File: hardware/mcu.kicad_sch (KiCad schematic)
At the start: 16 parts, among them U1 RP2350B, U2 W25Q128JVS, Y1 12MHz

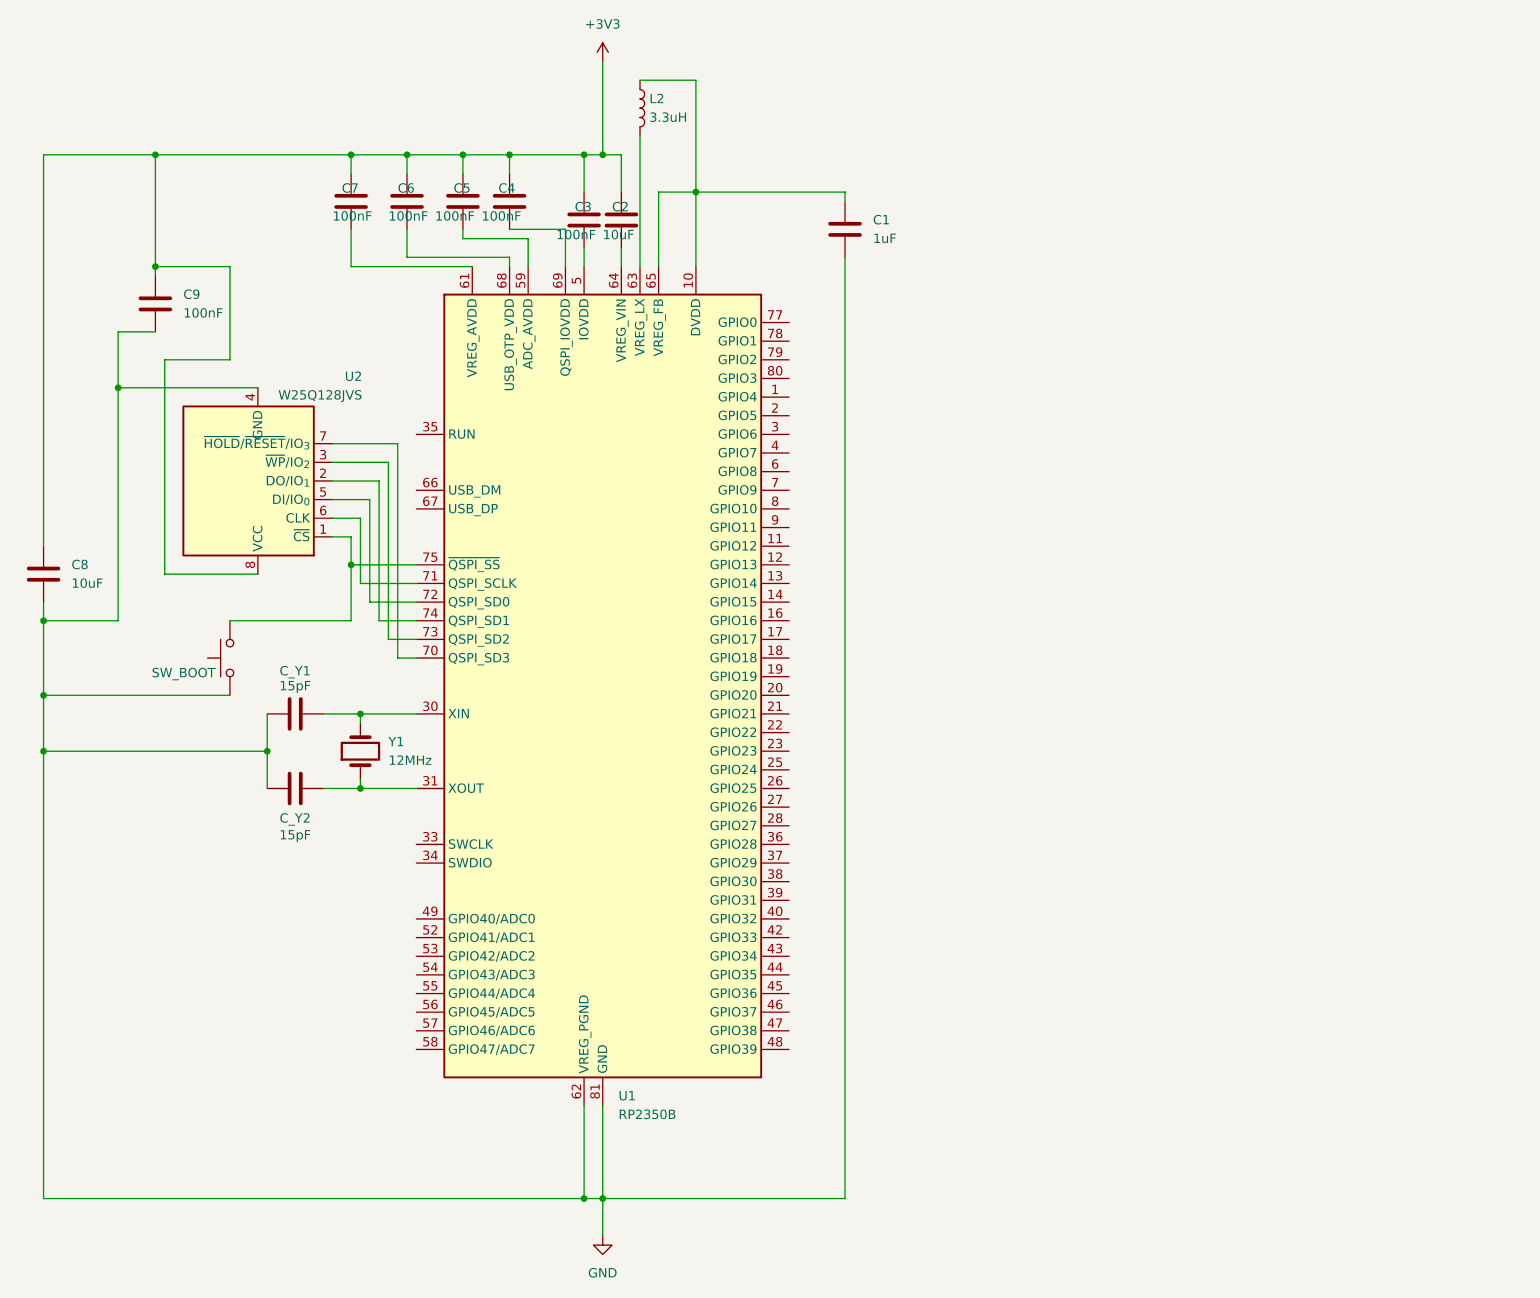
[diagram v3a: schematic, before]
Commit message: add I2C pullups
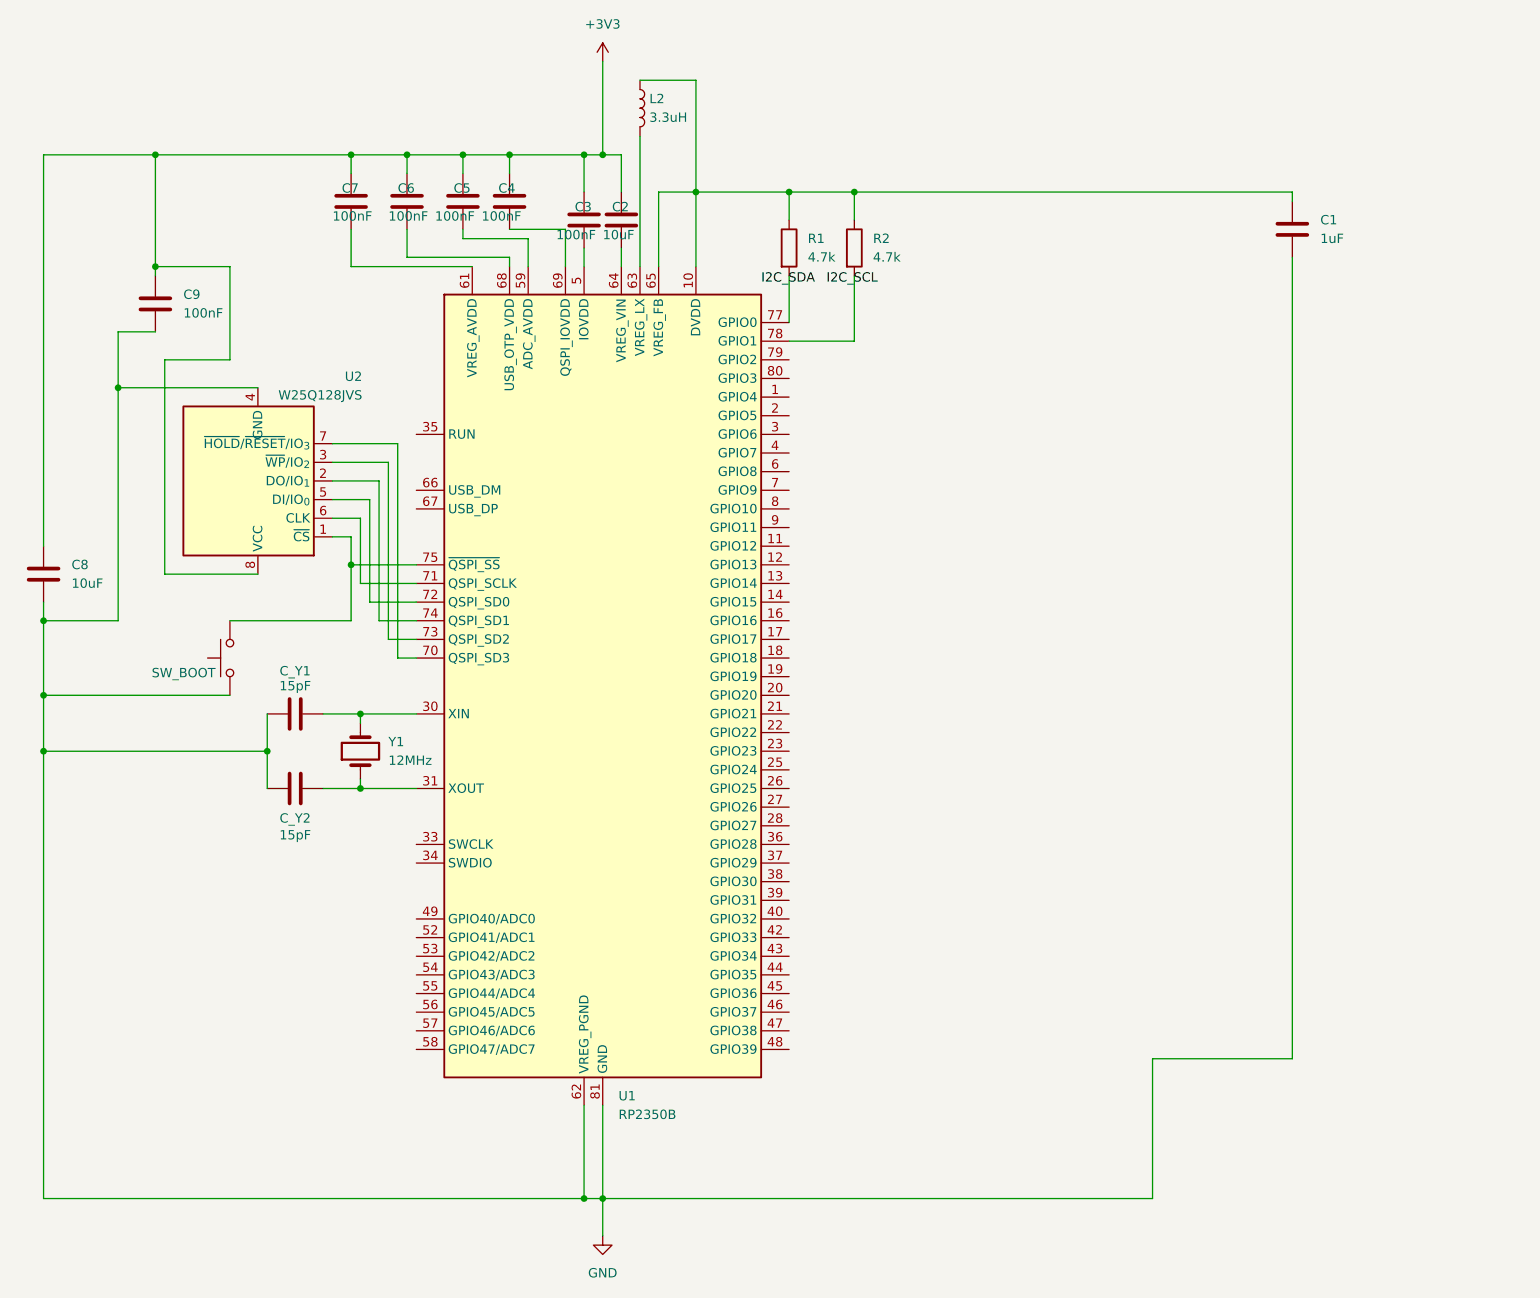
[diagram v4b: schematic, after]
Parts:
- added R1, R2: 4.7k, symbol Device:R
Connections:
- net at C1.1, L2.1, U1.10 (DVDD)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: now also R1.1, R2.1
- net at U1.77 (GPIO0): now also R1.2
- net at U1.78 (GPIO1): now also R2.2
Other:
- moved on the sheet: C1

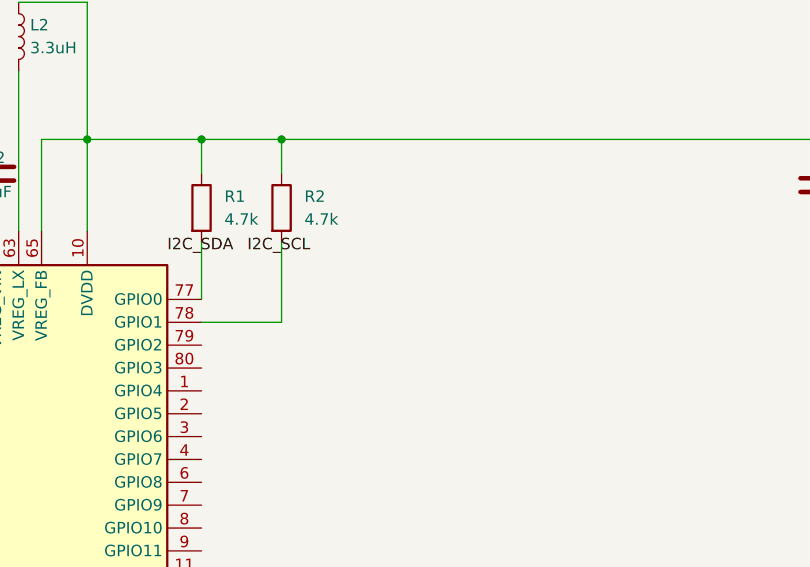
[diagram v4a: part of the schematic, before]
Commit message: add buck/boost
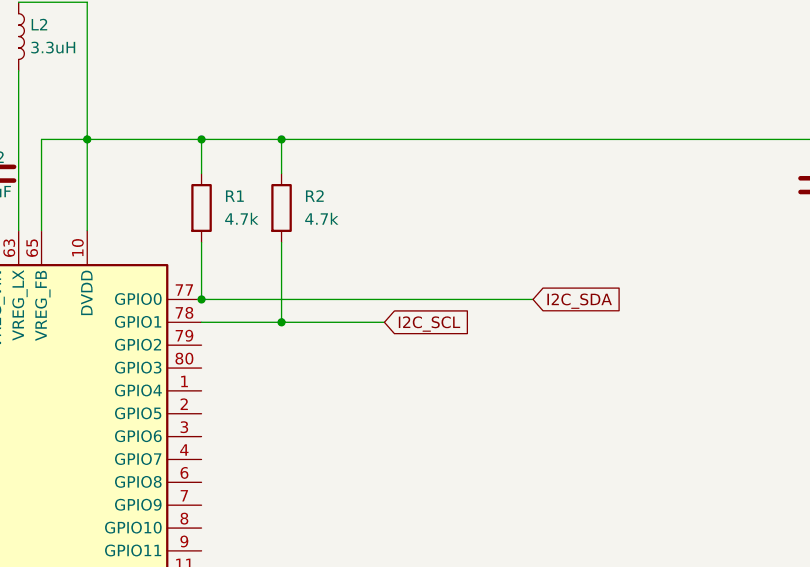
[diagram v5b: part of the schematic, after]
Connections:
- net I2C_SCL: now also R2.2, U1.78 (GPIO1)
- net I2C_SDA: now also R1.2, U1.77 (GPIO0)
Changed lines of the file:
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@@
+	)
+	(junction
+		(at 132.08 60.96)
+		(diameter 0)
+		(color 0 0 0 0)
 	)
 	(junction
@@
 	)
 	(junction
+		(at 123.19 58.42)
+		(diameter 0)
+		(color 0 0 0 0)
+	)
+	(junction
 		(at 85.09 35.56)
 		(diameter 0)
@@
 	(wire
 		(pts
+			(xy 132.08 60.96) (xy 143.51 60.96)
+		)
+		(stroke
+			(width 0)
+			(type default)
+		)
+	)
+	(wire
+		(pts
 			(xy 123.19 40.64) (xy 123.19 44.45)
 		)
@@
 	(wire
 		(pts
+			(xy 123.19 58.42) (xy 160.02 58.42)
+		)
+		(stroke
+			(width 0)
+			(type default)
+		)
+	)
+	(wire
+		(pts
 			(xy 67.31 80.01) (xy 67.31 99.06)
 		)
@@
 		)
 	)
-	(label "I2C_SCL"
-		(at 128.27 53.34 0)
+	(global_label "I2C_SCL"
+		(shape input)
+		(at 143.51 60.96 0)
+		(fields_autoplaced yes)
 		(effects
 			(font
 				(size 1.27 1.27)
 			)
-			(justify left bottom)
-		)
-	)
-	(label "I2C_SDA"
-		(at 119.38 53.34 0)
+			(justify left)
+		)
+		(property "Intersheetrefs" "${INTERSHEET_REFS}"
+			(at 154.0547 60.96 0)
+			(effects
+				(font
+					(size 1.27 1.27)
+				)
+				(justify left)
+				(hide yes)
+			)
+		)
+	)
+	(global_label "I2C_SDA"
+		(shape input)
+		(at 160.02 58.42 0)
+		(fields_autoplaced yes)
 		(effects
 			(font
 				(size 1.27 1.27)
 			)
-			(justify left bottom)
-		)
-	)
+			(justify left)
+		)
+		(property "Intersheetrefs" "${INTERSHEET_REFS}"
+			(at 170.6252 58.42 0)
+			(effects
+				(font
+					(size 1.27 1.27)
+				)
+				(justify left)
+				(hide yes)
+			)
+		)
+	)

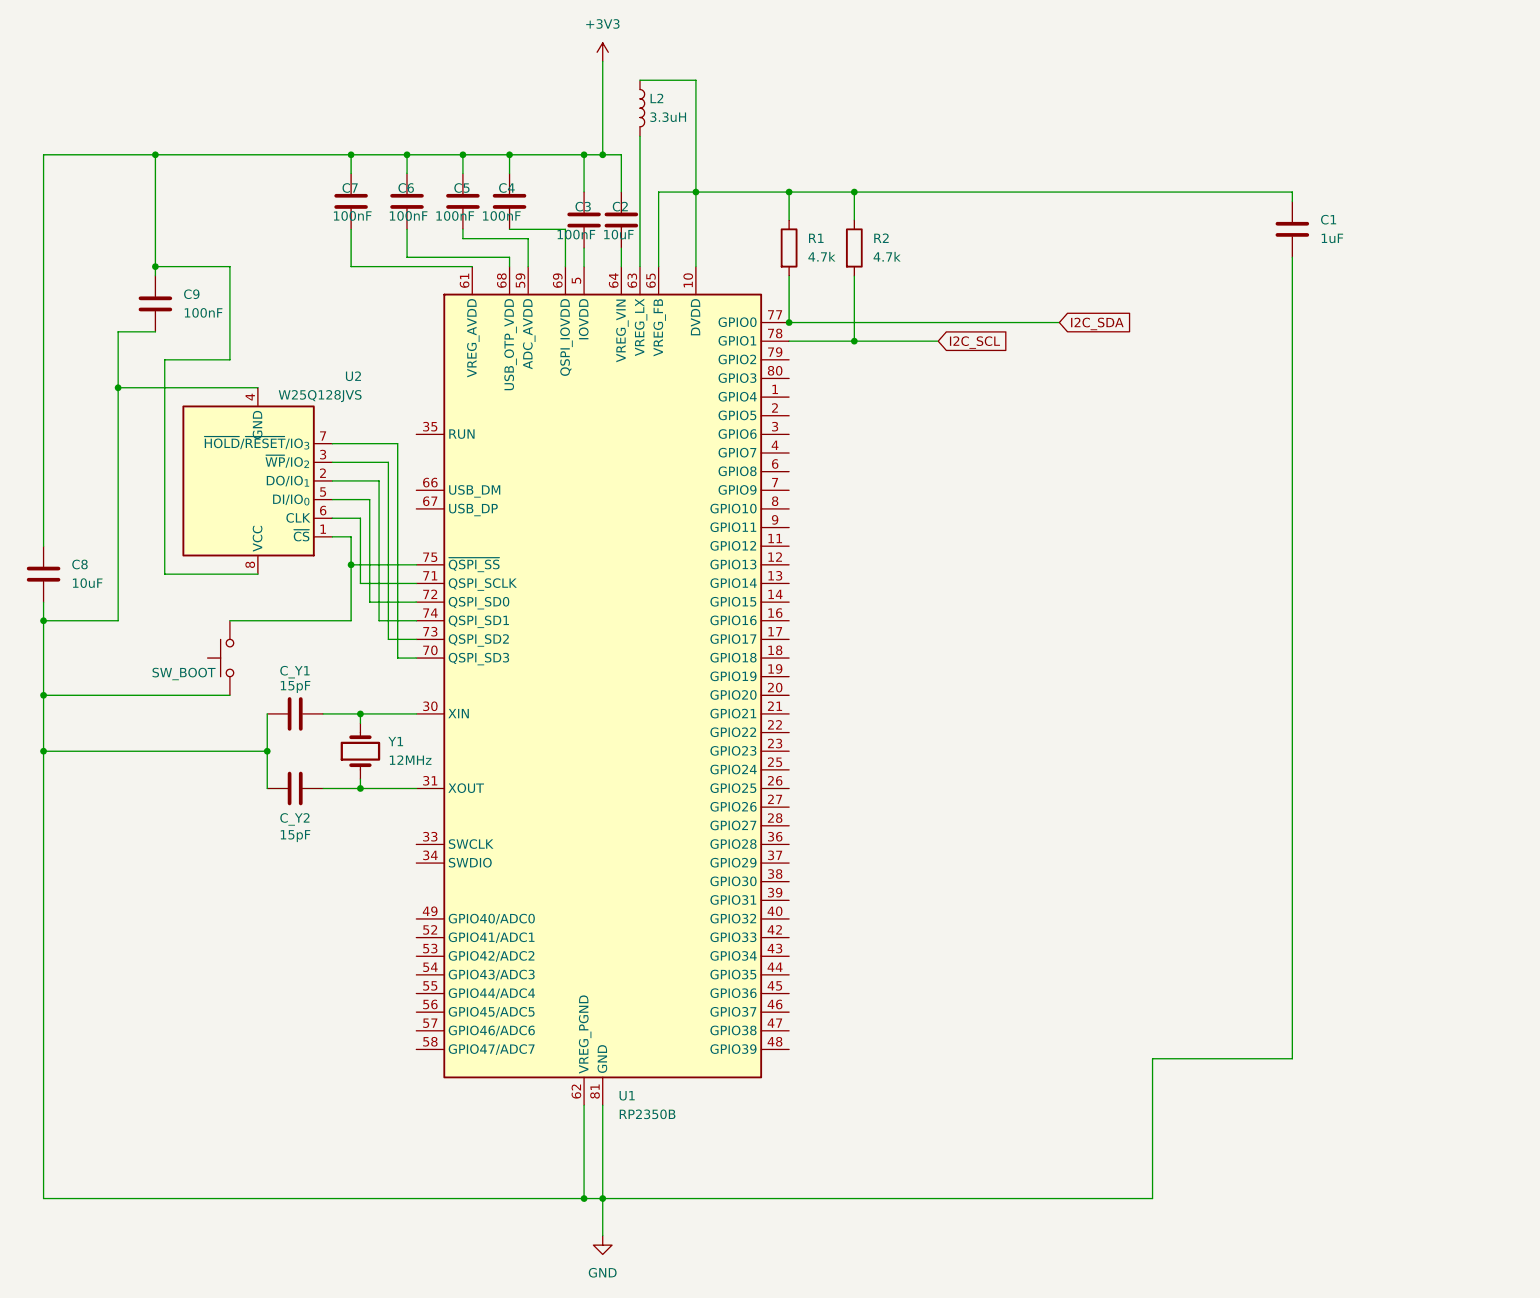
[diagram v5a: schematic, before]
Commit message: MCP GPIO pins to labels
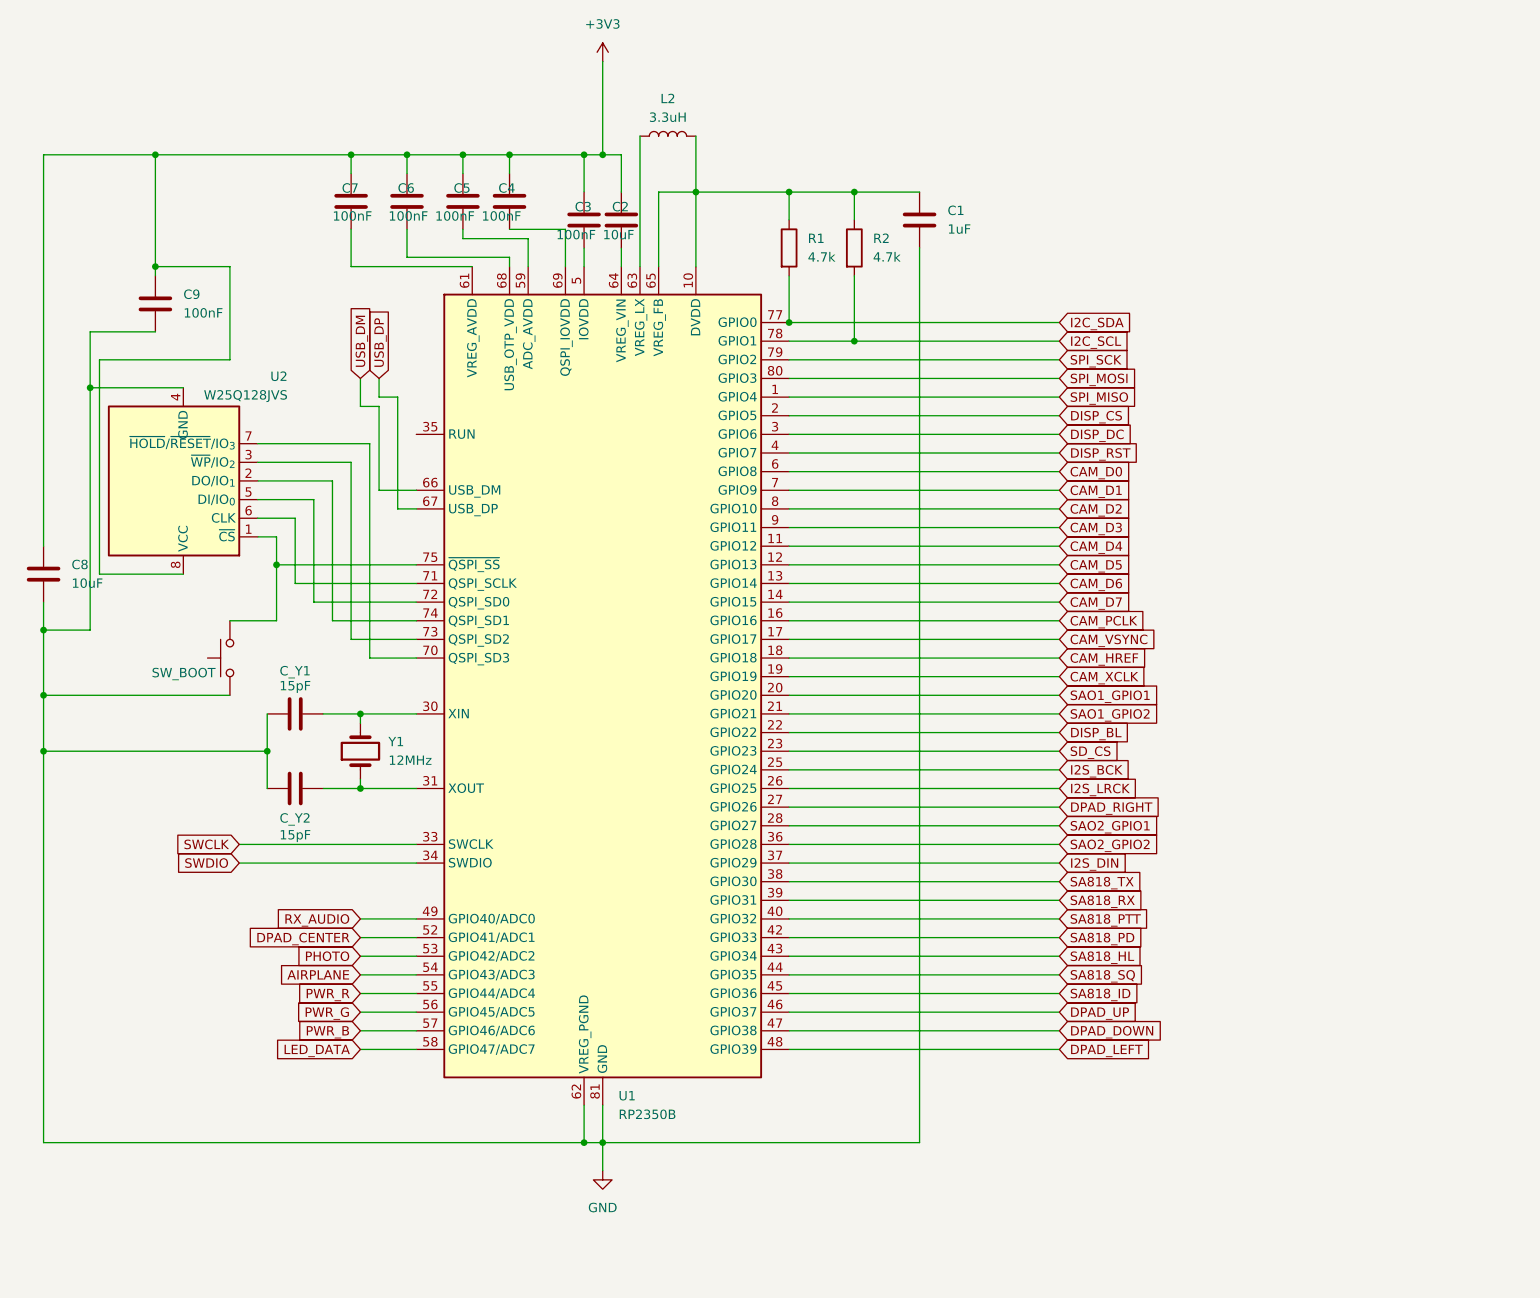
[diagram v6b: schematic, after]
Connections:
- net at C1.1, R1.1, R2.1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: now also L2.2; no longer L2.1
- net SPI_MISO: now reaches U1.1 (GPIO4)
- net CAM_D4: now reaches U1.11 (GPIO12)
- net CAM_D5: now reaches U1.12 (GPIO13)
- net CAM_D6: now reaches U1.13 (GPIO14)
- net CAM_D7: now reaches U1.14 (GPIO15)
- net CAM_PCLK: now reaches U1.16 (GPIO16)
- net CAM_VSYNC: now reaches U1.17 (GPIO17)
- net CAM_HREF: now reaches U1.18 (GPIO18)
- net CAM_XCLK: now reaches U1.19 (GPIO19)
- net DISP_CS: now reaches U1.2 (GPIO5)
- net SAO1_GPIO1: now reaches U1.20 (GPIO20)
- net SAO1_GPIO2: now reaches U1.21 (GPIO21)
- net DISP_BL: now reaches U1.22 (GPIO22)
- net SD_CS: now reaches U1.23 (GPIO23)
- net I2S_BCK: now reaches U1.25 (GPIO24)
- net I2S_LRCK: now reaches U1.26 (GPIO25)
- net DPAD_RIGHT: now reaches U1.27 (GPIO26)
- net SAO2_GPIO1: now reaches U1.28 (GPIO27)
- net DISP_DC: now reaches U1.3 (GPIO6)
- net SWCLK: now reaches U1.33 (SWCLK)
- net SWDIO: now reaches U1.34 (SWDIO)
- net SAO2_GPIO2: now reaches U1.36 (GPIO28)
- net I2S_DIN: now reaches U1.37 (GPIO29)
- net SA818_TX: now reaches U1.38 (GPIO30)
- net SA818_RX: now reaches U1.39 (GPIO31)
- net DISP_RST: now reaches U1.4 (GPIO7)
- net SA818_PTT: now reaches U1.40 (GPIO32)
- net SA818_PD: now reaches U1.42 (GPIO33)
- net SA818_HL: now reaches U1.43 (GPIO34)
- net SA818_SQ: now reaches U1.44 (GPIO35)
- net SA818_ID: now reaches U1.45 (GPIO36)
- net DPAD_UP: now reaches U1.46 (GPIO37)
- net DPAD_DOWN: now reaches U1.47 (GPIO38)
- net DPAD_LEFT: now reaches U1.48 (GPIO39)
- net RX_AUDIO: now reaches U1.49 (GPIO40/ADC0)
- net DPAD_CENTER: now reaches U1.52 (GPIO41/ADC1)
- net PHOTO: now reaches U1.53 (GPIO42/ADC2)
- net AIRPLANE: now reaches U1.54 (GPIO43/ADC3)
- net PWR_R: now reaches U1.55 (GPIO44/ADC4)
- net PWR_G: now reaches U1.56 (GPIO45/ADC5)
- net PWR_B: now reaches U1.57 (GPIO46/ADC6)
- net LED_DATA: now reaches U1.58 (GPIO47/ADC7)
- net CAM_D0: now reaches U1.6 (GPIO8)
- net at U1.63 (VREG_LX): now also L2.1; no longer L2.2
- net USB_DM: now reaches U1.66 (USB_DM)
- net USB_DP: now reaches U1.67 (USB_DP)
- net CAM_D1: now reaches U1.7 (GPIO9)
- net SPI_SCK: now reaches U1.79 (GPIO2)
- net CAM_D2: now reaches U1.8 (GPIO10)
- net SPI_MOSI: now reaches U1.80 (GPIO3)
- net CAM_D3: now reaches U1.9 (GPIO11)
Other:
- moved on the sheet: C1, L2, U2
